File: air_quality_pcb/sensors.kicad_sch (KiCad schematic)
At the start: 18 parts, among them IC1 SCD41-D-R2, IC2 SGP41-D-R4, J2 52435-2871, U2 MQ-6, U3 MQ-6

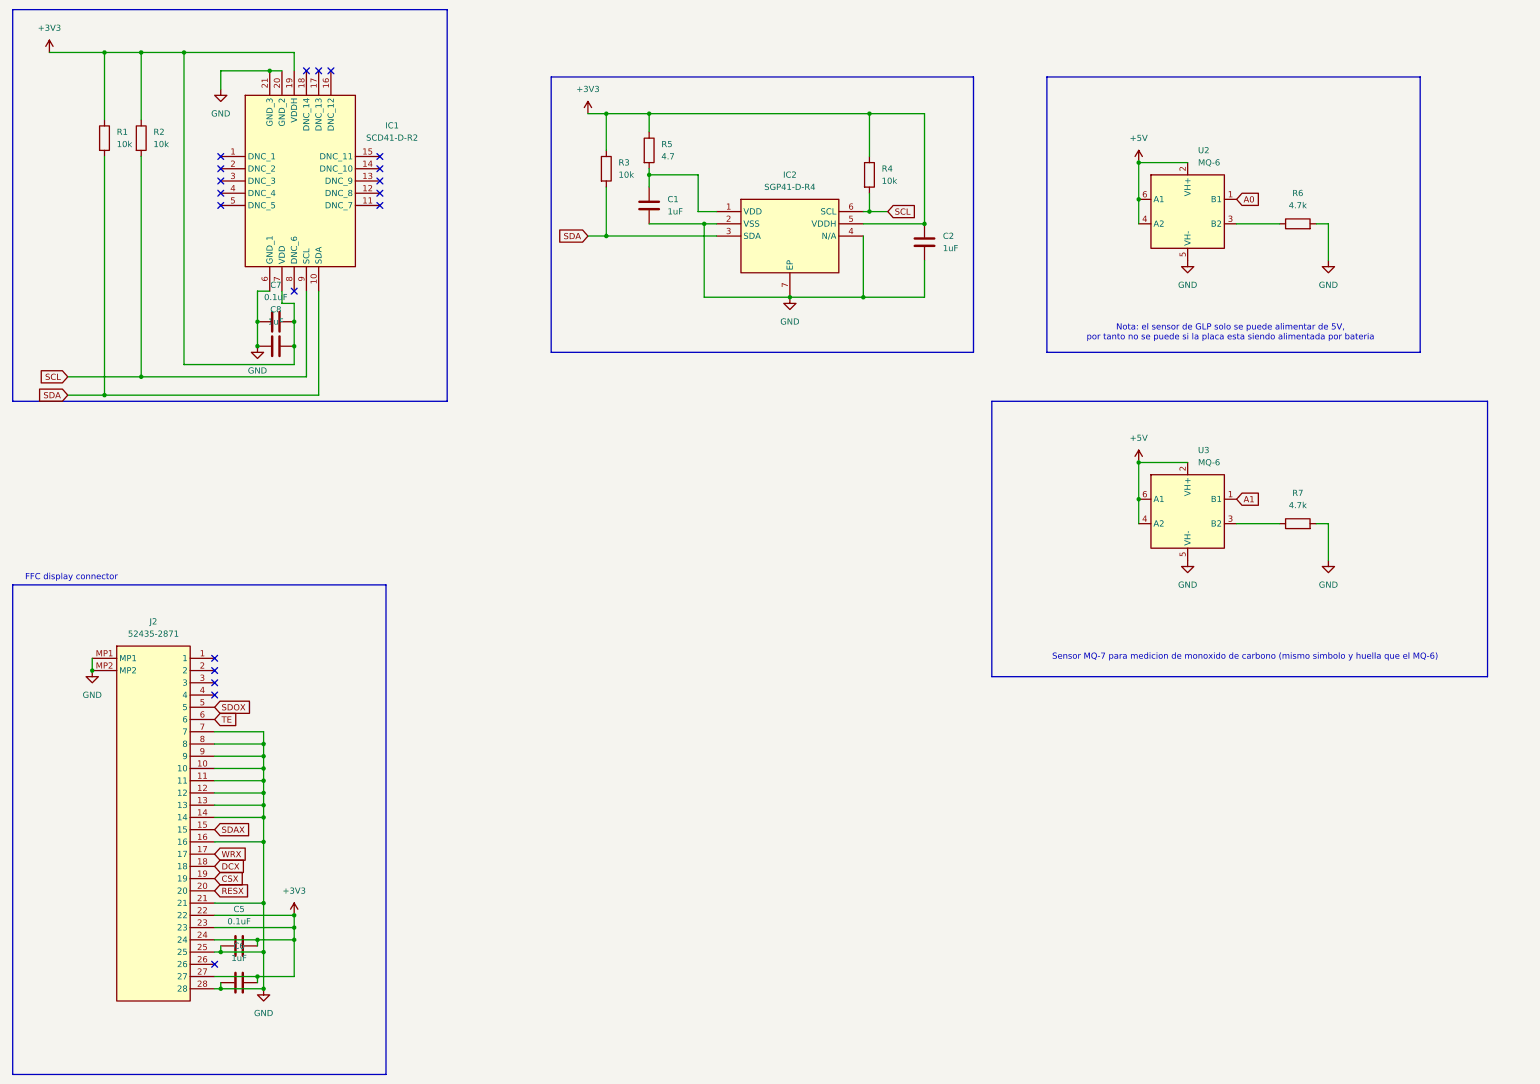
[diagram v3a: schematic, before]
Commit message: added buck boost for 5v battery powered
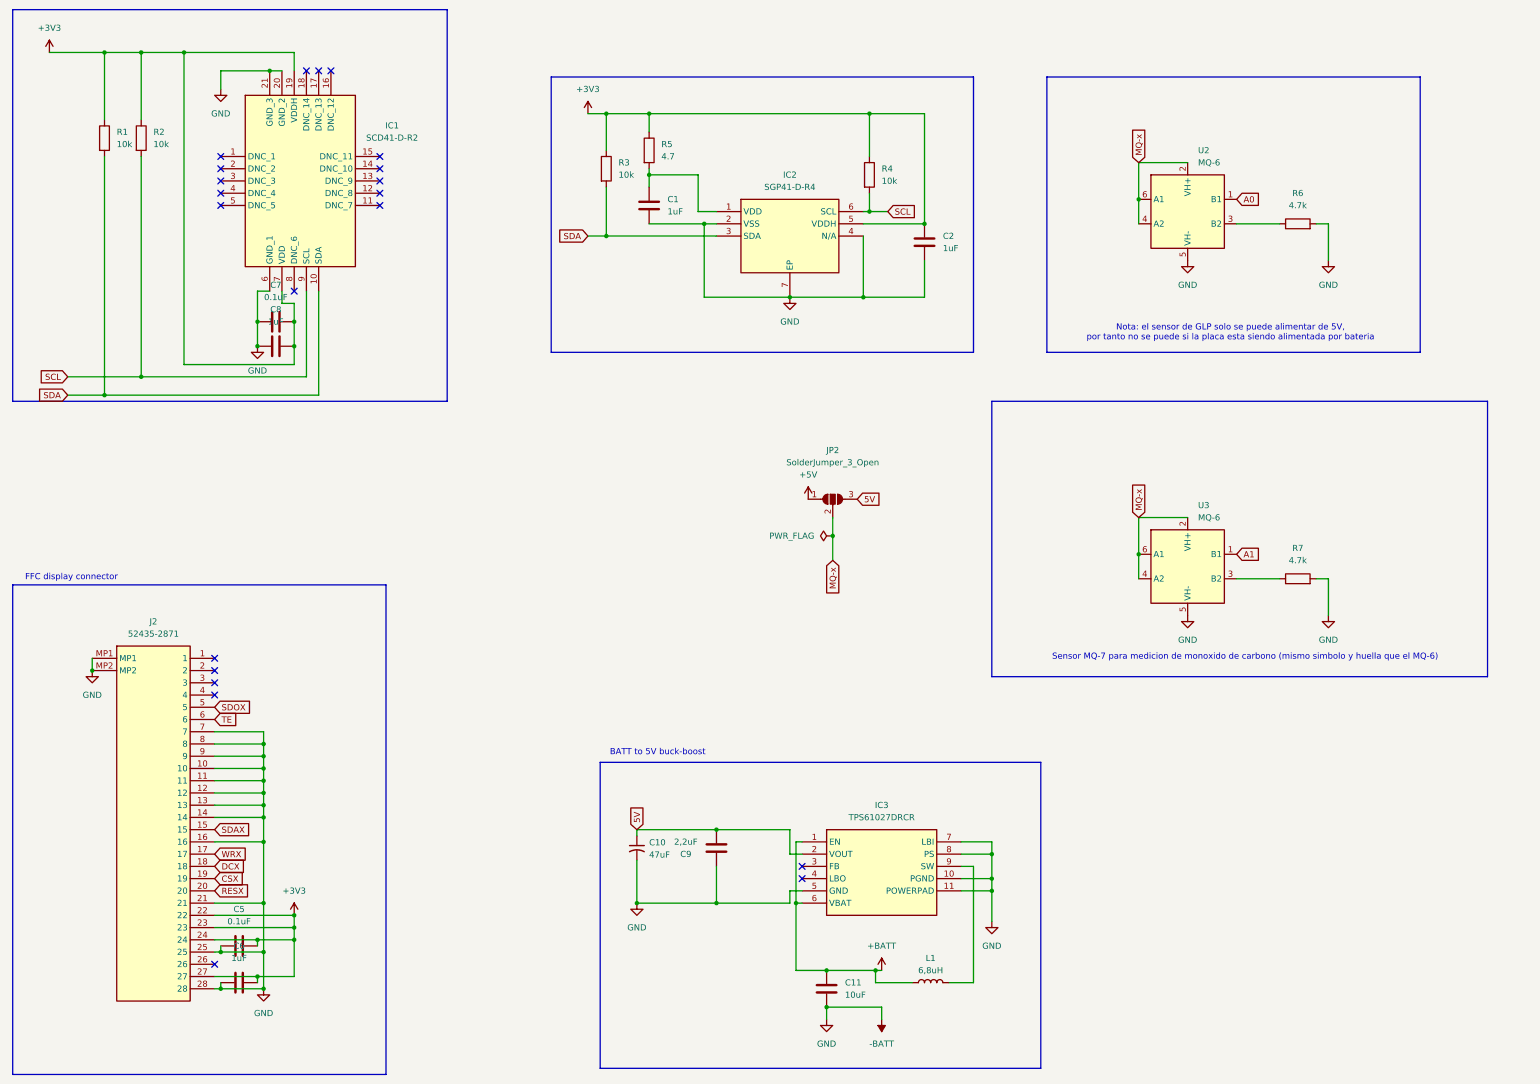
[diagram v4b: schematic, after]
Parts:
- added C10: 47uF, project_extras:CAPPM3216X180N, symbol Device:C_Small_US
- added C11: 10uF, Capacitor_SMD:C_1206_3216Metric, symbol Device:C
- added C9: 2,2uF, Capacitor_SMD:C_1206_3216Metric, symbol Device:C
- added IC3: TPS61027DRCR, project_extras:TPS74901DRCR, symbol project_extras:TPS61027DRCR
- added JP2: SolderJumper_3_Open, Jumper:SolderJumper-3_P1.3mm_Open_RoundedPad1.0x1.5mm_NumberLabels, symbol Jumper:SolderJumper_3_Open
- added L1: 6,8uH, project_extras:INDPM6363X300N, symbol Device:L
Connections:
- net +5V: now also JP2.1 (A); no longer U2.2 (VH+), U2.4 (A2), U2.6 (A1), U3.2 (VH+), U3.4 (A2), U3.6 (A1)
- net GND renamed -BATT
- net -BATT: now also C10.2, C11.1, C9.2, IC3.10 (PGND), IC3.11 (POWERPAD), IC3.5 (GND), IC3.7 (LBI), IC3.8 (PS)
- new net: IC3.9 (SW), L1.2
- new net +BATT: C11.2, IC3.1 (EN), IC3.6 (VBAT), L1.1
- new net 5V: C10.1, C9.1, IC3.2 (VOUT), JP2.3 (B)
- new net MQ-x: JP2.2 (C), U2.2 (VH+), U2.4 (A2), U2.6 (A1), U3.2 (VH+), U3.4 (A2), U3.6 (A1)
- no-connect marks 19 -> 21
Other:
- note added: "BATT to 5V buck-boost"
- moved on the sheet: R7, U3

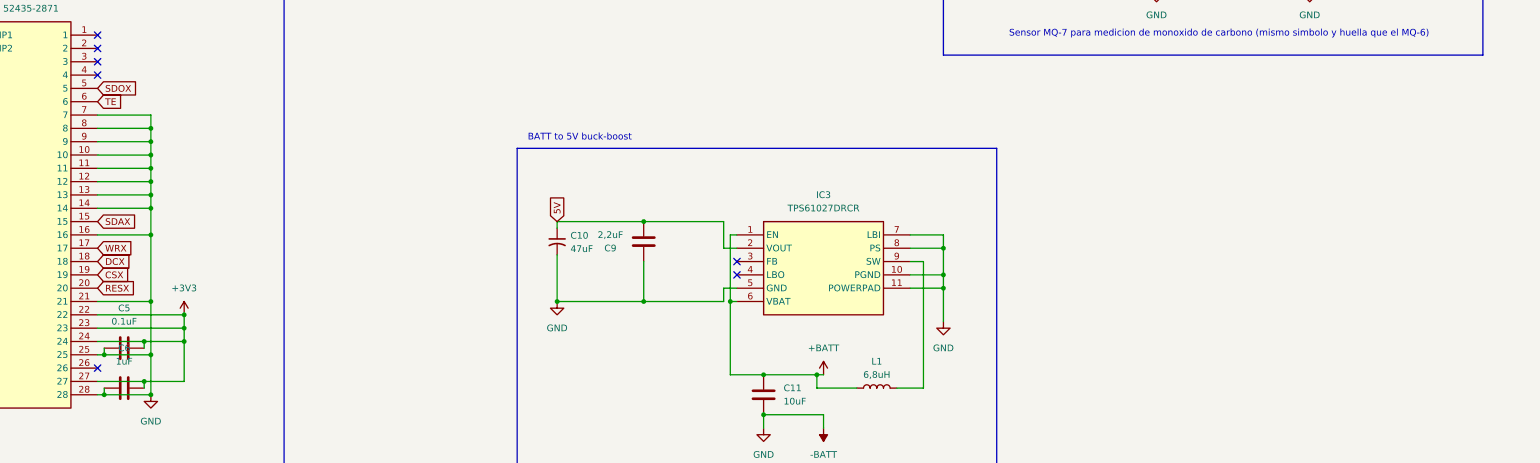
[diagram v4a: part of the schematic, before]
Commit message: added buzzer
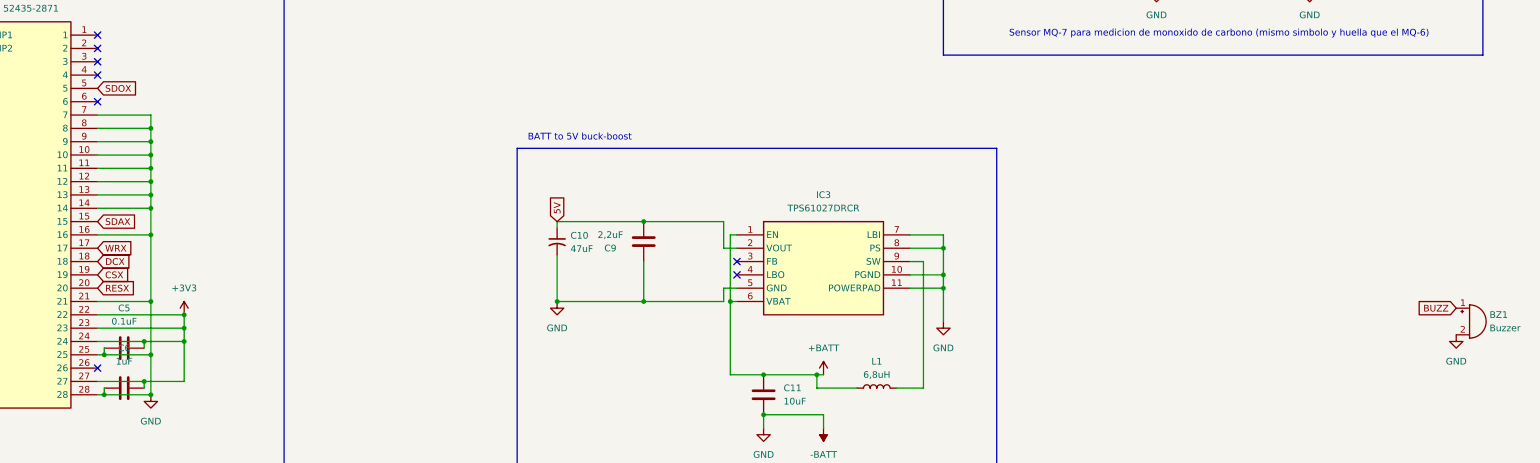
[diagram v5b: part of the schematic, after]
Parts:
- added BZ1: Buzzer, Buzzer_Beeper:Buzzer_12x9.5RM7.6, symbol Device:Buzzer
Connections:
- net -BATT: now also BZ1.2 (-)
- net TE: no longer names the net of J2.6
- new net BUZZ: BZ1.1 (+)
- no-connect marks 21 -> 22
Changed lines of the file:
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@@
 	)
 	(no_connect
+		(at 85.09 172.72)
+	)
+	(no_connect
 		(at 86.36 66.04)
 	)
@@
 		)
 	)
-	(global_label "TE"
+	(global_label "SCL"
 		(shape input)
-		(at 85.09 172.72 0)
+		(at 224.79 67.31 0)
 		(fields_autoplaced yes)
 		(effects
@@
 		)
 		(property "Intersheetrefs" "${INTERSHEET_REFS}"
-			(at 90.1918 172.72 0)
+			(at 231.2828 67.31 0)
 			(effects
 				(font
@@
 		)
 	)
-	(global_label "SCL"
+	(global_label "SDOX"
 		(shape input)
-		(at 224.79 67.31 0)
+		(at 85.09 170.18 0)
 		(fields_autoplaced yes)
 		(effects
@@
 		)
 		(property "Intersheetrefs" "${INTERSHEET_REFS}"
-			(at 231.2828 67.31 0)
+			(at 93.0947 170.18 0)
 			(effects
 				(font
@@
 		)
 	)
-	(global_label "SDOX"
+	(global_label "BUZZ"
 		(shape input)
-		(at 85.09 170.18 0)
+		(at 344.17 212.09 180)
 		(fields_autoplaced yes)
 		(effects
@@
 				(size 1.27 1.27)
 			)
-			(justify left)
+			(justify right)
 		)
 		(property "Intersheetrefs" "${INTERSHEET_REFS}"
-			(at 93.0947 170.18 0)
+			(at 336.1653 212.09 0)
 			(effects
 				(font
 					(size 1.27 1.27)
 				)
-				(justify left)
+				(justify right)
 				(hide yes)
 			)
@@
 	)
 	(symbol
+		(lib_id "Device:Buzzer")
+		(at 346.71 214.63 0)
+		(unit 1)
+		(exclude_from_sim no)
+		(in_bom yes)
+		(on_board yes)
+		(dnp no)
+		(fields_autoplaced yes)
+		(property "Reference" "BZ1"
+			(at 350.52 213.3599 0)
+			(effects
+				(font
+					(size 1.27 1.27)
+				)
+				(justify left)
+			)
+		)
+		(property "Value" "Buzzer"
+			(at 350.52 215.8999 0)
+			(effects
+				(font
+					(size 1.27 1.27)
+				)
+				(justify left)
+			)
+		)
+		(property "Footprint" "Buzzer_Beeper:Buzzer_12x9.5RM7.6"
+			(at 346.075 212.09 90)
+			(effects
+				(font
+					(size 1.27 1.27)
+				)
+				(hide yes)
+			)
+		)
+		(property "Datasheet" "~"
+			(at 346.075 212.09 90)
+			(effects
+				(font
+					(size 1.27 1.27)
+				)
+				(hide yes)
+			)
+		)
+		(property "Description" "Buzzer, polarized"
+			(at 346.71 214.63 0)
+			(effects
+				(font
+					(size 1.27 1.27)
+				)
+				(hide yes)
+			)
+		)
+		(pin "2"
+		)
+		(pin "1"
+		)
+		(instances
+			(project "air_quality_pcb"
+				(path "/be1998fb-5191-483f-bd03-46c23a7136b7/b27140a6-bcb9-424e-b527-20251a6eb7b3"
+					(reference "BZ1")
+					(unit 1)
+				)
+			)
+		)
+	)
+	(symbol
 		(lib_id "power:GND")
 		(at 212.09 234.95 0)
@@
 					(unit 1)
 				)
+			)
+		)
+	)
+	(symbol
+		(lib_id "power:GND")
+		(at 344.17 217.17 0)
+		(unit 1)
+		(exclude_from_sim no)
+		(in_bom yes)
+		(on_board yes)
+		(dnp no)
+		(fields_autoplaced yes)
+		(property "Reference" "#PWR013"
+			(at 344.17 223.52 0)
+			(effects
+				(font
+					(size 1.27 1.27)
+				)
+				(hide yes)
+			)
+		)
+		(property "Value" "GND"
+			(at 344.17 222.25 0)
+			(effects
+				(font
+					(size 1.27 1.27)
+				)
+			)
+		)
+		(property "Footprint" ""
+			(at 344.17 217.17 0)
+			(effects
+				(font
+					(size 1.27 1.27)
+				)
+				(hide yes)
+			)
+		)
+		(property "Datasheet" ""
+			(at 344.17 217.17 0)
+			(effects
+				(font
+					(size 1.27 1.27)
+				)
+				(hide yes)
+			)
+		)
+		(property "Description" "Power symbol creates a global label with name \"GND\" , ground"
+			(at 344.17 217.17 0)
+			(effects
+				(font
+					(size 1.27 1.27)
+				)
+				(hide yes)
+			)
+		)
+		(pin "1"
+		)
+		(instances
+			(project "air_quality_pcb"
+				(path "/be1998fb-5191-483f-bd03-46c23a7136b7/b27140a6-bcb9-424e-b527-20251a6eb7b3"
+					(reference "#PWR013")
+					(unit 1)
+				)
